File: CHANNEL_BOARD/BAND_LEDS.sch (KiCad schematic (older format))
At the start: 17 parts, among them Q1 MMBTA42, U3 TL074

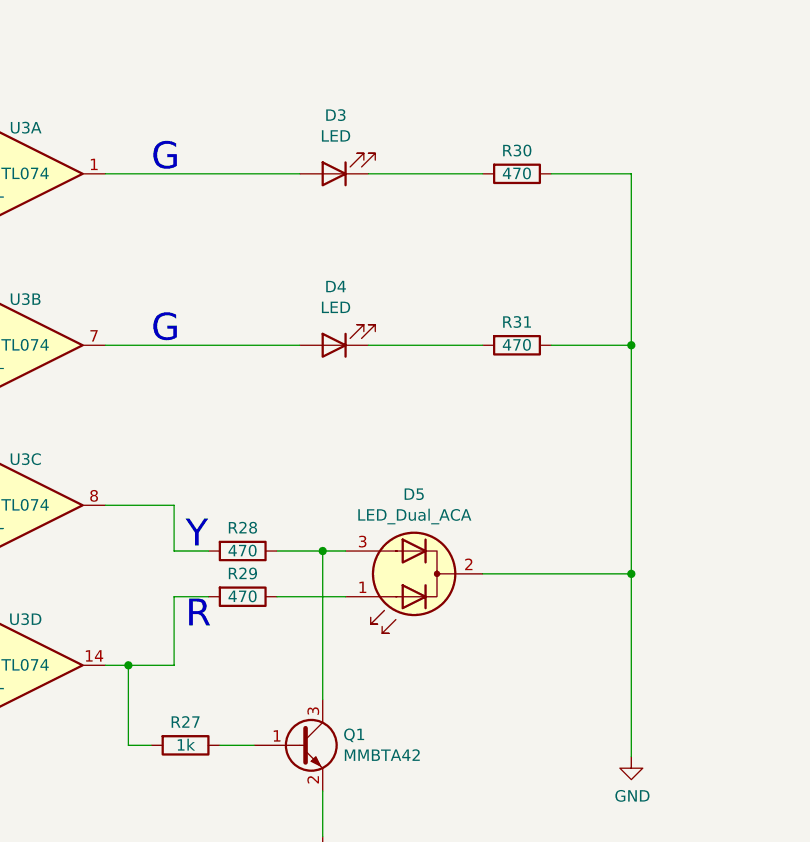
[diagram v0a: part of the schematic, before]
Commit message: New series resistor values for LEDs
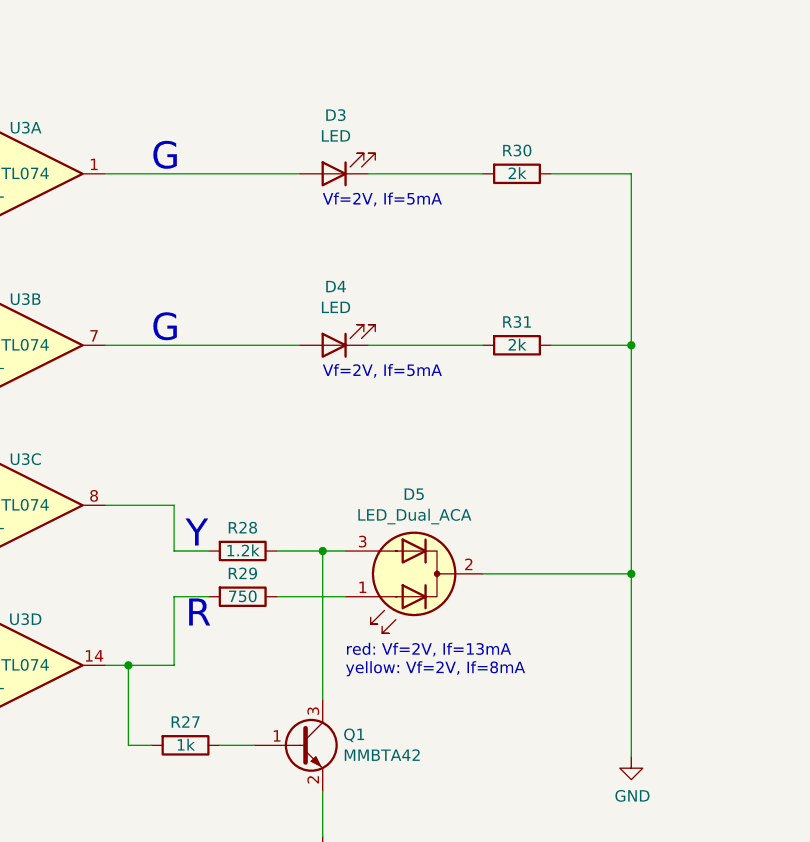
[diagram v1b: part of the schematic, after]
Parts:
- R28: value 470 -> 1.2k
- R29: value 470 -> 750
- R30, R31: value 470 -> 2k
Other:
- note added: "Vf=2V, If=5mA"
- note added: "red: Vf=2V, If=13mA\nyellow: Vf=2V, If=8mA"
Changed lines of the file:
@@
 AR Path="/617C2B43/60A371D0" Ref="R30"  Part="1"
 F 0 "R30" V 5150 2050 50  0000 C CNN
-F 1 "470" V 5250 2050 50  0000 C CNN
+F 1 "2k" V 5250 2050 50  0000 C CNN
 F 2 "Resistor_SMD:R_0603_1608Metric_Pad0.98x0.95mm_HandSolder" V 5180 2050 50  0001 C CNN
 F 3 "~" H 5250 2050 50  0001 C CNN
@@
 AR Path="/617C2B43/60A37A90" Ref="R31"  Part="1"
 F 0 "R31" V 5150 2800 50  0000 C CNN
-F 1 "470" V 5250 2800 50  0000 C CNN
+F 1 "2k" V 5250 2800 50  0000 C CNN
 F 2 "Resistor_SMD:R_0603_1608Metric_Pad0.98x0.95mm_HandSolder" V 5180 2800 50  0001 C CNN
 F 3 "~" H 5250 2800 50  0001 C CNN
@@
 AR Path="/617C2B43/60A37D88" Ref="R28"  Part="1"
 F 0 "R28" V 3950 3700 50  0000 C CNN
-F 1 "470" V 4050 3700 50  0000 C CNN
+F 1 "1.2k" V 4050 3700 50  0000 C CNN
 F 2 "Resistor_SMD:R_0603_1608Metric_Pad0.98x0.95mm_HandSolder" V 3980 3700 50  0001 C CNN
 F 3 "~" H 4050 3700 50  0001 C CNN
@@
 AR Path="/617C2B43/60A38334" Ref="R29"  Part="1"
 F 0 "R29" V 3950 3900 50  0000 C CNN
-F 1 "470" V 4050 3900 50  0000 C CNN
+F 1 "750" V 4050 3900 50  0000 C CNN
 F 2 "Resistor_SMD:R_0603_1608Metric_Pad0.98x0.95mm_HandSolder" V 3980 3900 50  0001 C CNN
 F 3 "~" H 4050 3900 50  0001 C CNN
@@
 	1    0    0    -1
 $EndComp
+Text Notes 4400 2200 0    50   ~ 0
+Vf=2V, If=5mA
+Text Notes 4400 2950 0    50   ~ 0
+Vf=2V, If=5mA
+Text Notes 4500 4250 0    50   ~ 0
+red: Vf=2V, If=13mA\nyellow: Vf=2V, If=8mA
 $EndSCHEMATC
